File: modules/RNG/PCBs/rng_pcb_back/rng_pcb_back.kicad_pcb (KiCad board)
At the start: 2 copper layers, 50 x 100 mm, 35 parts, among them J1 Conn_01x07_Socket, J10 Conn_01x08_Socket, J11 Eurorack_2x8_Power, J8 Conn_02x03_Socket, J9 Conn_01x06_Socket, U1 TLC5940NT, U2 MCP4922, U3 MCP6004, U4 TL072, U5 LM4040BIZ-5, U6 TLC5940PWP

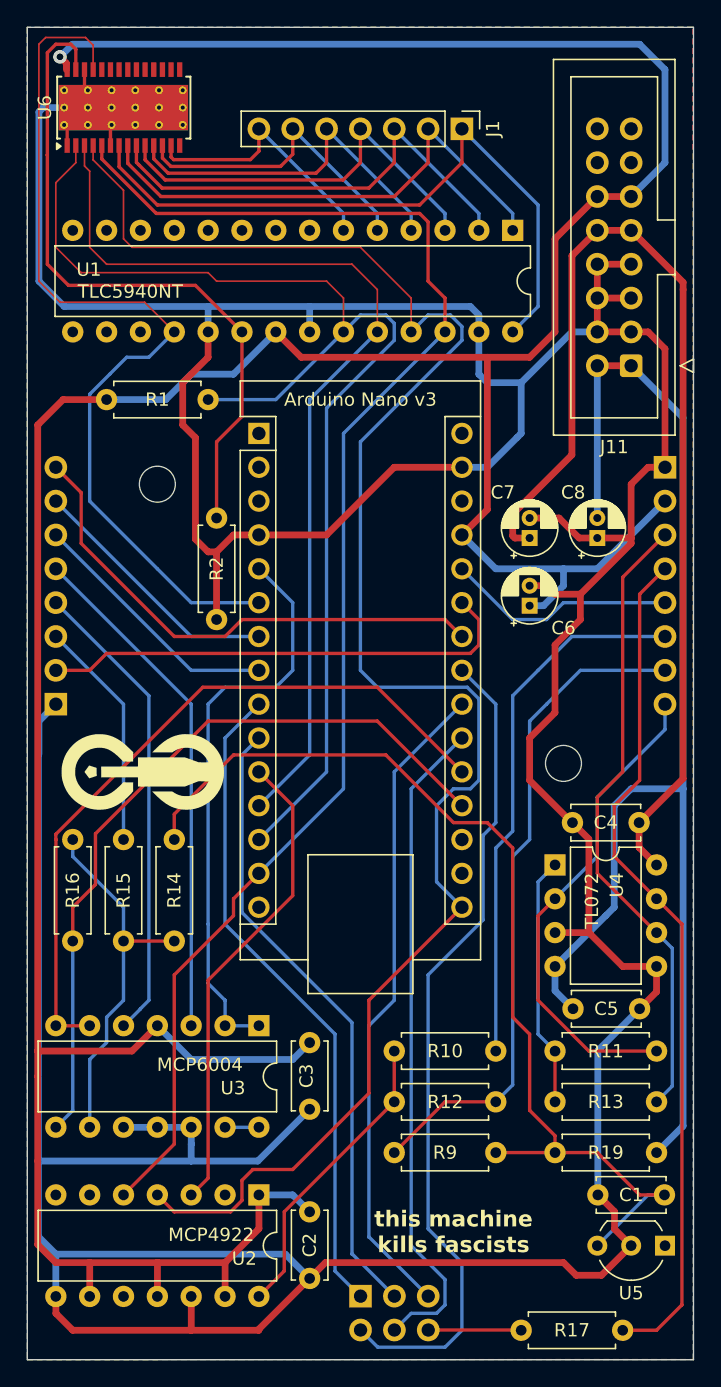
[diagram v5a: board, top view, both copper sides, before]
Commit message: Fix #55 and add decoupling capacitors
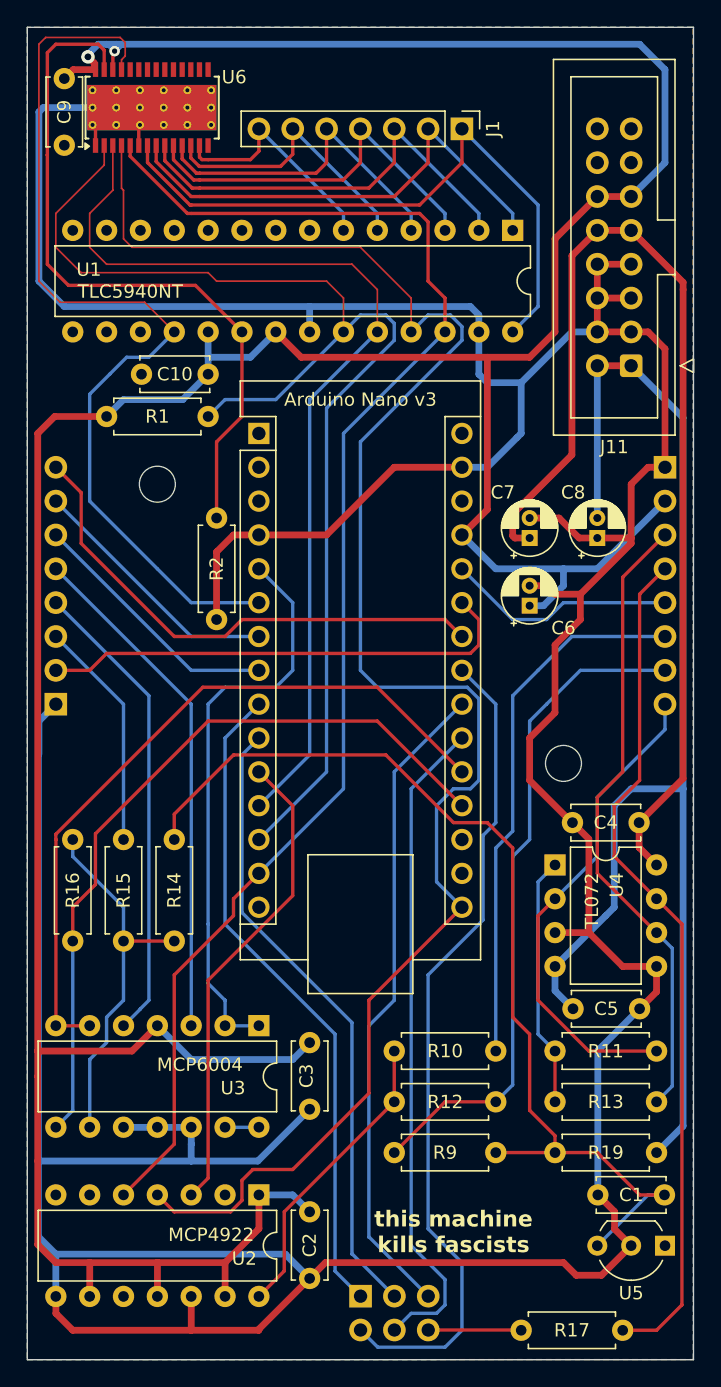
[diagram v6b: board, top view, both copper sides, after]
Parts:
- removed G1: logo_small, FreeModular:logo_small
- added C10: 100nF, Capacitor_THT:C_Disc_D5.0mm_W2.5mm_P5.00mm, F.Cu at (39.4, 76.8)
- added C9: 100nF, Capacitor_THT:C_Disc_D5.0mm_W2.5mm_P5.00mm, F.Cu at (28.6, 54.6)
- moved U6 2.13 mm to (35.1, 56.8)
- moved R1 1.27 mm to (39.4, 80.0)
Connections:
- U1 pad 19: GND -> +5V
- U6 pad 26: GND -> +5V
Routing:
- net GND: track 383.9 -> 363.7 mm
- net +5V: track 269.6 -> 276.3 mm, vias 1 -> 2
- net LED_PWM_REF: track 68.0 -> 70.7 mm
- net /Led Driver/LED_1: track 50.8 -> 48.4 mm
- net /Led Driver/LED_3: track 35.1 -> 32.8 mm
- net SPI_MOSI: track 111.0 -> 108.8 mm
- net /Led Driver/LED_2: track 38.7 -> 36.5 mm
- net /Led Driver/LED_5: track 27.5 -> 25.4 mm
- net /Led Driver/LED_6: track 23.5 -> 21.4 mm
- net /Led Driver/LED_4: track 31.2 -> 29.1 mm
- net /Led Driver/LED_7: track 19.7 -> 17.6 mm
- net /Led Driver/IREF: track 51.4 -> 53.5 mm
- net LED_BLANK: track 93.8 -> 95.2 mm
- net SPI_SCK: track 133.7 -> 132.8 mm

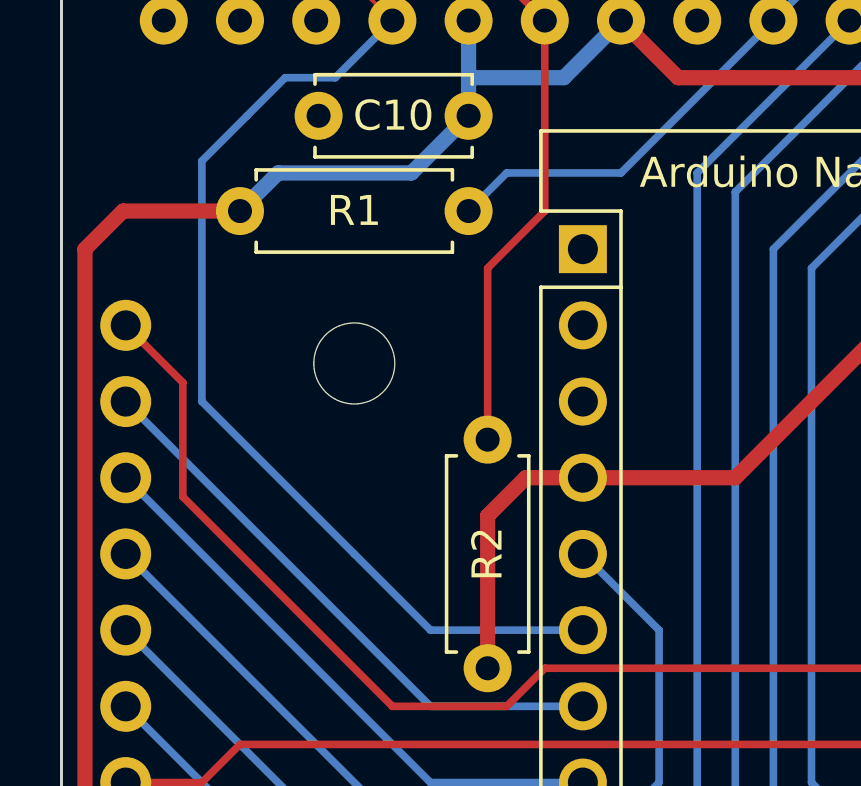
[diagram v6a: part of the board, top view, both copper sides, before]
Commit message: Fix wrong resistor designators on RNG
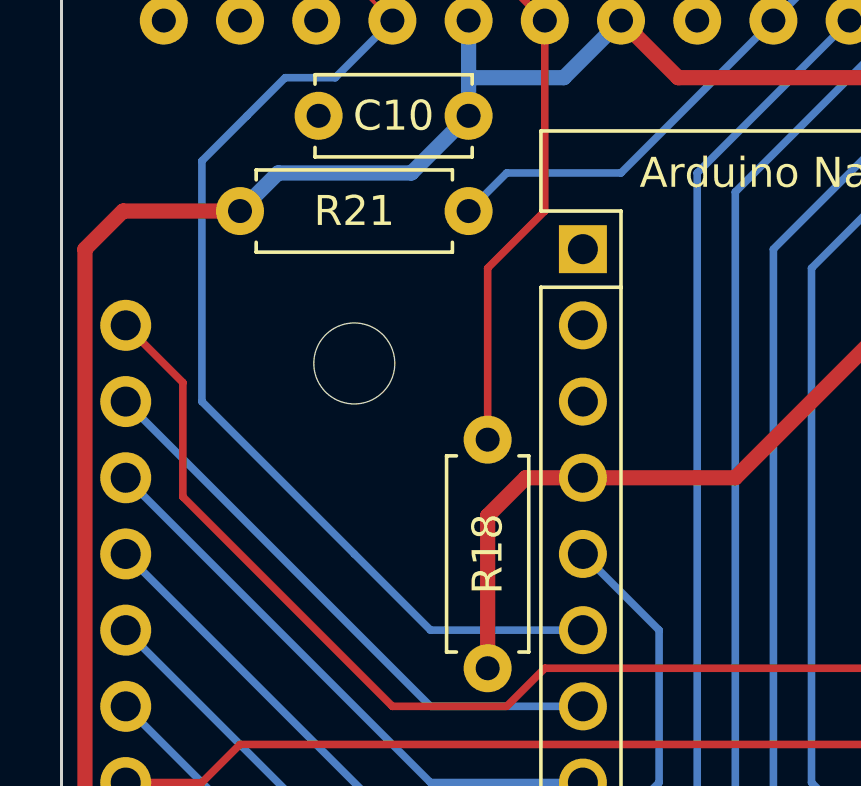
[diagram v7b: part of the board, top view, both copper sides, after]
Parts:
- removed R1: 100kΩ, Resistor_THT:R_Axial_DIN0207_L6.3mm_D2.5mm_P7.62mm_Horizontal
- removed R2: 15kΩ, Resistor_THT:R_Axial_DIN0207_L6.3mm_D2.5mm_P7.62mm_Horizontal
- added R18: 15kΩ, Resistor_THT:R_Axial_DIN0207_L6.3mm_D2.5mm_P7.62mm_Horizontal, F.Cu at (40.0, 87.6)
- added R21: 100kΩ, Resistor_THT:R_Axial_DIN0207_L6.3mm_D2.5mm_P7.62mm_Horizontal, F.Cu at (39.4, 80.0)
